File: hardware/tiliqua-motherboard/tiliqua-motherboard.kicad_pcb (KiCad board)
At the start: 6 copper layers, 31.7 x 110 mm, 154 parts, among them J1 Conn_01x15, J10 DVI_GPDI, J2 Conn_02x06_Top_Bottom, J3 Conn_02x06_Top_Bottom, J5 USB_C_Receptacle_USB2.0_14P, J6 CONN 2x5 P=2.54mm, J7 USB_C_Receptacle_USB2.0_14P, J8 MICROMOD-2222, SW2 SW_Tactile_SPST, SW3 RotaryEncoder_Switch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

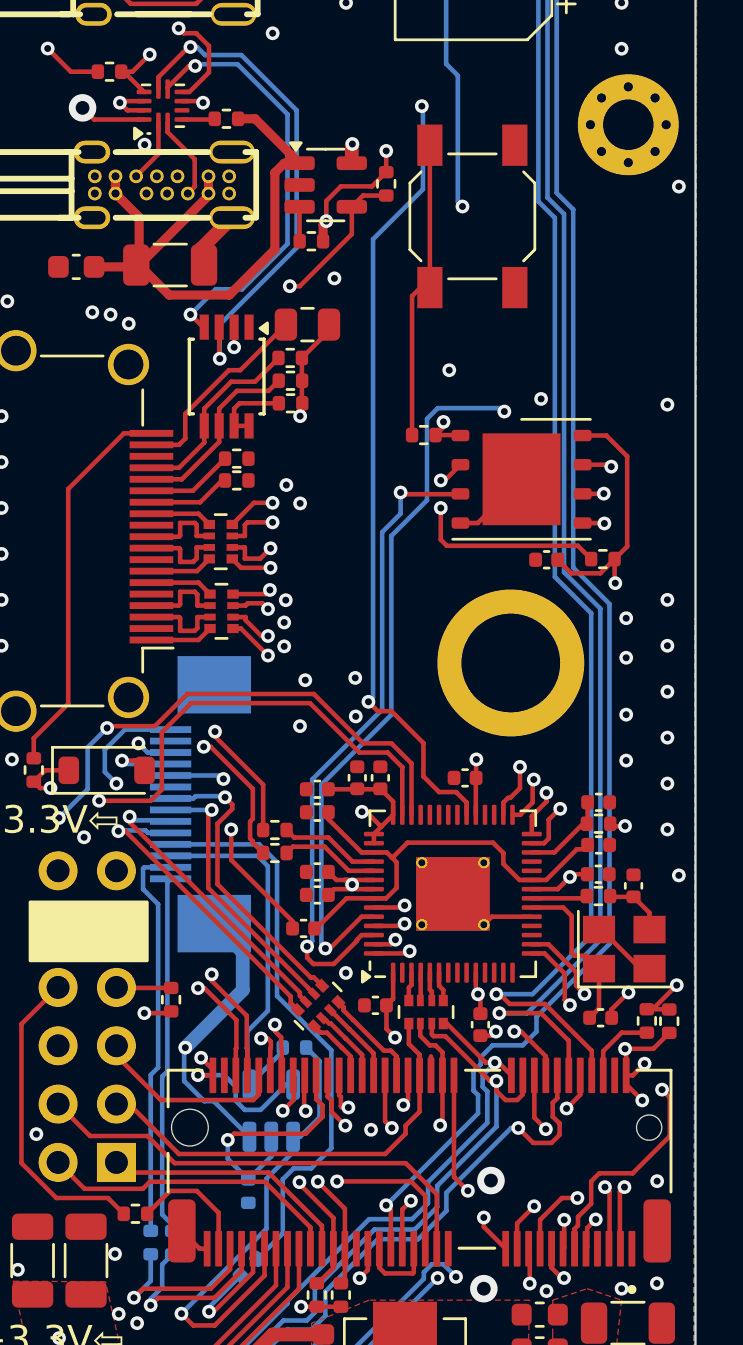
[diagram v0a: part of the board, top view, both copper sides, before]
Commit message: * cleaner DVI routing / USB2 layerswap
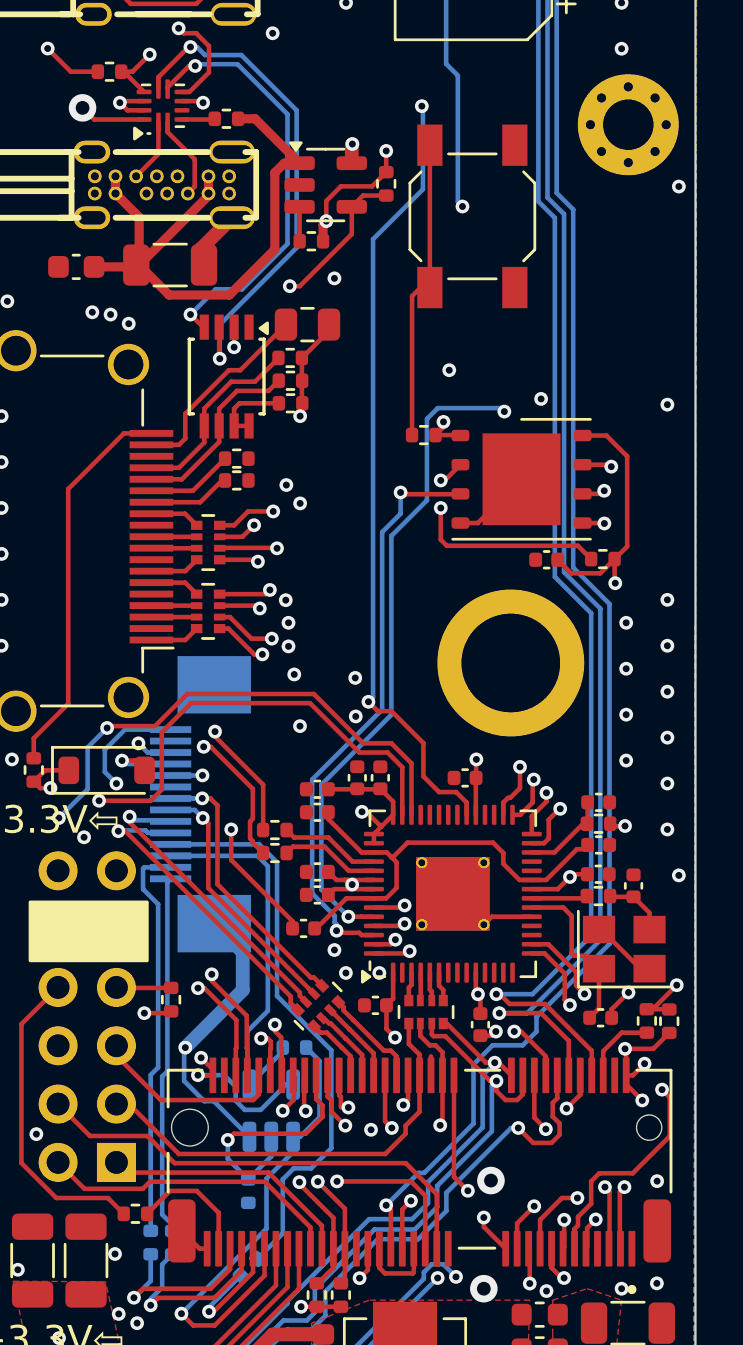
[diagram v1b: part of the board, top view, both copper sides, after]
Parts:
- moved RN6 0.58 mm to (10.4, 45.0)
- moved RN7 0.55 mm to (10.4, 42.0)
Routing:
- net Net-(U12-IO2): track 28.2 -> 25.5 mm
- net Net-(U12-CLK): track 38.1 -> 35.6 mm
- net Net-(U12-DO(IO1)): track 24.5 -> 26.5 mm
- net Net-(U12-IO3): track 29.9 -> 31.7 mm
- net /gpdi/CONN_D2-: track 3.65 -> 1.97 mm
- net /gpdi/CONN_D1+: track 3.65 -> 1.97 mm
- net /gpdi/CONN_D0-: track 3.64 -> 1.98 mm
- net /gpdi/CONN_CK+: track 3.61 -> 1.98 mm
- net Net-(U12-DI(IO0)): track 28.4 -> 30.0 mm
- net GPDI_D2+: track 35.4 -> 34.1 mm
- net Net-(U12-~{CS}): track 38.1 -> 39.2 mm
- net GPDI_D2-: track 35.4 -> 34.3 mm
- net FFC_SDIN1: track 13.0 -> 12.0 mm
- net +3V3: track 128.5 -> 127.5 mm
- net GPDI_D0-: track 35.6 -> 34.8 mm
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
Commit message: * update DNP entries, add nlnet logo
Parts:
- added G***: LOGO, LOGO, F.Cu at (14.9, 18.9)
- added G***: LOGO, LOGO, B.Cu at (28.9, 31.2)
- R34, R35, R36, R37, R38, R39, R47, R48, R49: value 27R -> 33R
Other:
- board text added: "R4/01.25"
- board text removed: "R4/12.24"

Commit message: * fab 05.01.24
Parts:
- added R40: 33R, Resistor_SMD:R_0402_1005Metric, F.Cu at (12.7, 49.3)
- added R41: 33R, Resistor_SMD:R_0402_1005Metric, F.Cu at (12.7, 48.3)
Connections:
- U2 pad 40: MOBO_I2C_SDA -> /rp2040_jtag/I2C0_SDA
- U2 pad 41: MOBO_I2C_SCL -> /rp2040_jtag/I2C0_SCL
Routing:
- net +3V3: track 127.5 -> 108.2 mm
- net ENC_B: track 89.6 -> 73.4 mm, vias 2 -> 3
- net ENC_S: track 92.9 -> 81.0 mm, vias 2 -> 3
- net MOBO_I2C_SDA: track 149.6 -> 139.1 mm
- net MOBO_I2C_SCL: track 154.5 -> 144.8 mm
- net /rp2040_jtag/I2C0_SDA: track 0.00 -> 9.61 mm
- net /rp2040_jtag/I2C0_SCL: track 0.00 -> 9.04 mm
- net ENC_A: track 77.8 -> 76.3 mm, vias 2 -> 3
- net Net-(U12-CLK): track 35.6 -> 34.2 mm, vias 3 -> 4
- net USB_VBUS_EN: track 83.4 -> 82.4 mm
- net GND: vias 108 -> 128
